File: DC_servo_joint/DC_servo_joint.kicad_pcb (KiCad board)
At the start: 2 copper layers, 6 parts, among them J1 12401598E4_2A, J2 B2B-XH-A_LF__SN_, U1 DRV8871DDA, U2 ESP32-C3-WROOM-02, U3 MT6701CT, U4 LM1117MP-3.3

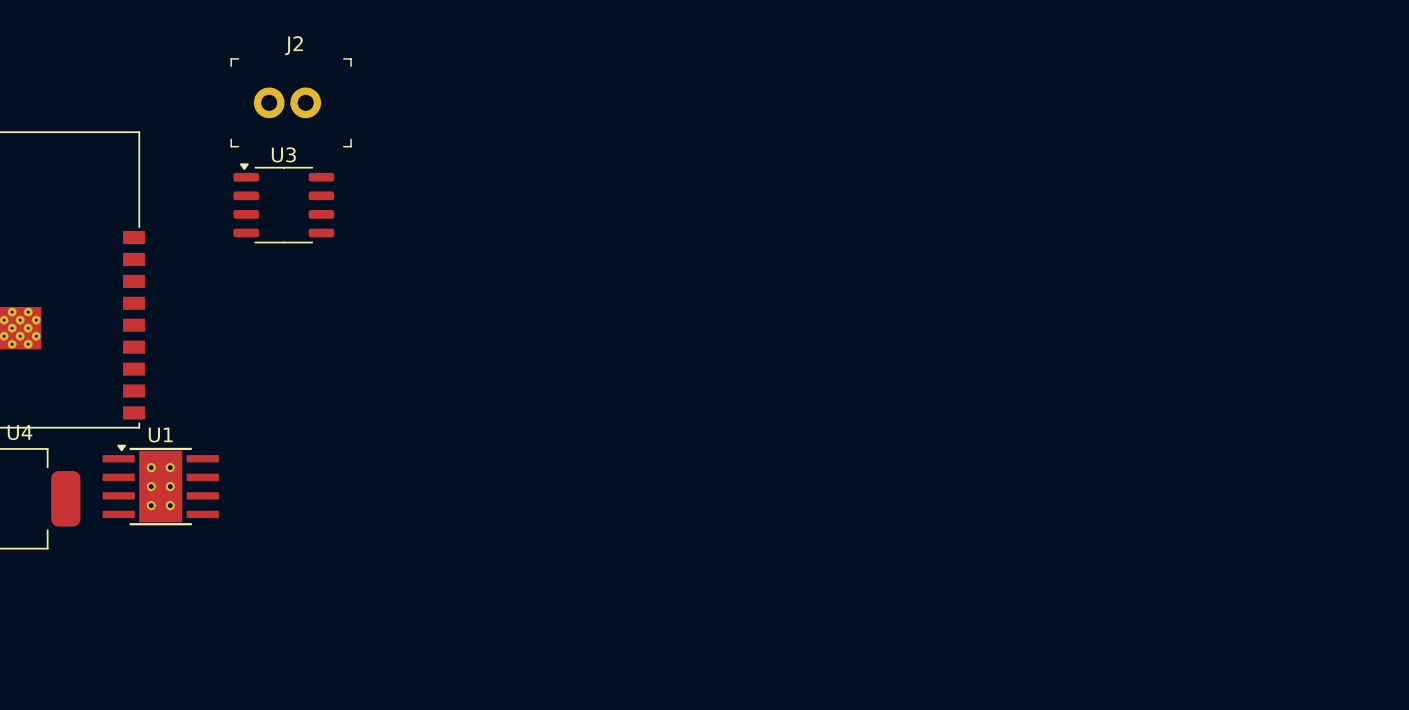
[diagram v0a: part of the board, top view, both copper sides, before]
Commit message: Update the usb header to 8 pins,
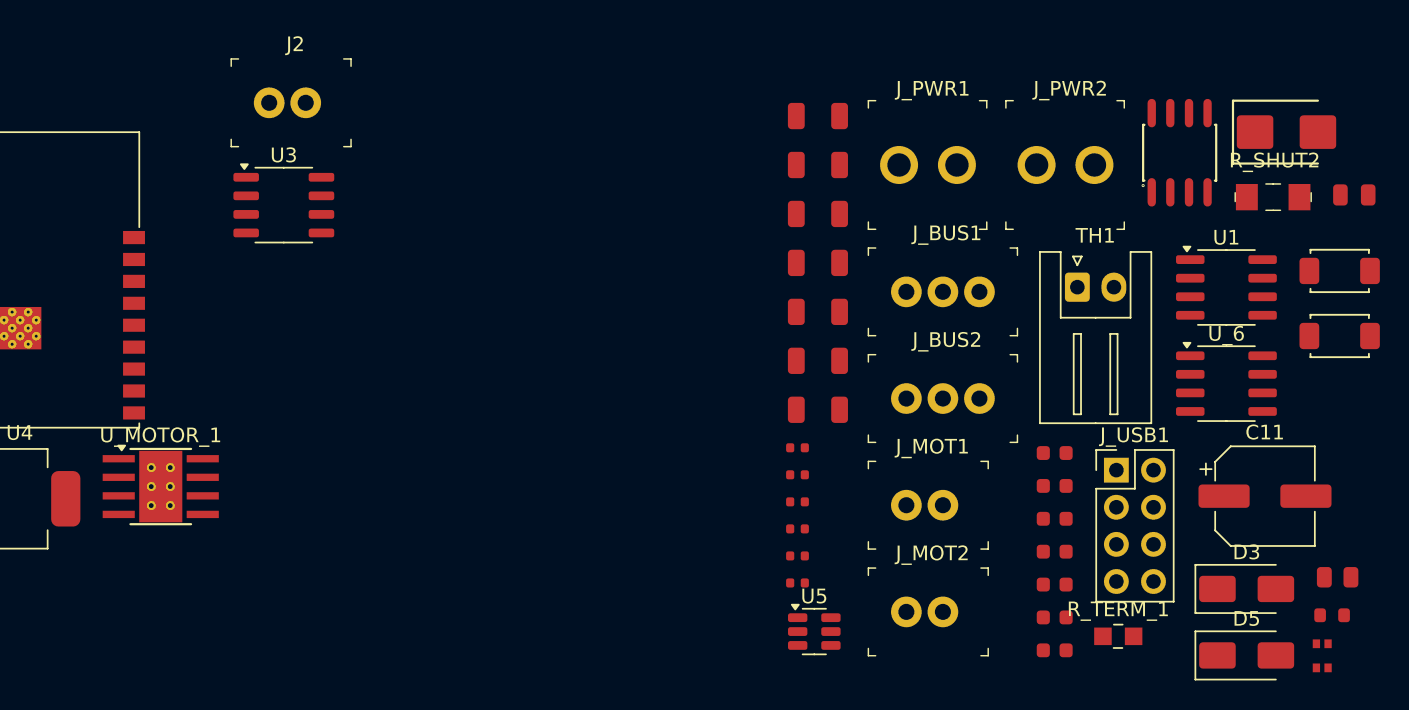
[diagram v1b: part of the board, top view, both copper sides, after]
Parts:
- added C1: 4.7uF, PCM_JLCPCB:C_1206, F.Cu at (190.6, 77.7)
- added C10: 22uF, PCM_JLCPCB:C_1206, F.Cu at (190.6, 94.5)
- added C11: 47uf, Capacitor_SMD:CP_Elec_6.3x5.4, F.Cu at (221.2, 103.8)
- added C12: 100nF, PCM_JLCPCB:C_0603, F.Cu at (206.8, 109.8)
- added C13: 100nF, PCM_JLCPCB:C_0603, F.Cu at (206.8, 112.0)
- added C14: 10uF, PCM_JLCPCB:C_0805, F.Cu at (227.3, 83.1)
- added C16: 100nF, PCM_JLCPCB:C_0603, F.Cu at (206.8, 114.3)
- added C17: 4.7uF, PCM_JLCPCB:C_1206, F.Cu at (190.6, 97.8)
- added C2: 220nF, PCM_JLCPCB:C_1206, F.Cu at (190.6, 81.1)
- added C3: 22uF, PCM_JLCPCB:C_1206, F.Cu at (190.6, 84.4)
- added C4: 100nF, PCM_JLCPCB:C_0603, F.Cu at (206.8, 100.8)
- added C5: 100nF, PCM_JLCPCB:C_1206, F.Cu at (190.6, 87.8)
- added C6: 100nF, PCM_JLCPCB:C_0603, F.Cu at (206.8, 103.0)
- added C7: 100nF, PCM_JLCPCB:C_0603, F.Cu at (206.8, 105.3)
- added C8: 10nF, PCM_JLCPCB:C_0603, F.Cu at (206.8, 107.5)
- added C9: 10uF, PCM_JLCPCB:C_1206, F.Cu at (190.6, 91.1)
- added D1: SMBJ6.5CA, PCM_JLCPCB:D_SMB, F.Cu at (222.7, 78.8)
- added D2: H15VL10B, PCM_JLCPCB:D_DFN1006-2L, F.Cu at (225.1, 113.8)
- added D3: SS34, Diode_SMD:D_SMA, F.Cu at (219.9, 110.1)
- added D4: H15VL10B, PCM_JLCPCB:D_DFN1006-2L, F.Cu at (225.1, 115.5)
- added D5: SS34, Diode_SMD:D_SMA, F.Cu at (219.9, 114.7)
- added J_BUS1: B3B-XH-A_LF__SN_, digikey-footprints:PinHeader_1x3_P2.5mm_Drill1.1mm, F.Cu at (196.6, 89.8)
- added J_BUS2: B3B-XH-A_LF__SN_, digikey-footprints:PinHeader_1x3_P2.5mm_Drill1.1mm, F.Cu at (196.6, 97.1)
- added J_MOT1: B2B-XH-A_LF__SN_, digikey-footprints:PinHeader_1x2_P2.5mm_Drill1.1mm, F.Cu at (196.6, 104.4)
- added J_MOT2: B2B-XH-A_LF__SN_, digikey-footprints:PinHeader_1x2_P2.5mm_Drill1.1mm, F.Cu at (196.6, 111.7)
- added J_PWR1: B2P-VH_LF__SN_, digikey-footprints:PinHeader_1x2_P3.96mm_Drill1.6mm, F.Cu at (196.1, 81.1)
- added J_PWR2: B2P-VH_LF__SN_, digikey-footprints:PinHeader_1x2_P3.96mm_Drill1.6mm, F.Cu at (205.6, 81.1)
- added J_USB1: USB_PAD, Connector_PinHeader_2.54mm:PinHeader_2x04_P2.54mm_Vertical, F.Cu at (211.0, 102.0)
- added R1: 33kΩ, PCM_JLCPCB:R_0402, F.Cu at (189.2, 100.4)
- added R2: 10kΩ, PCM_JLCPCB:R_0402, F.Cu at (189.2, 102.3)
- added R3: 68kΩ, PCM_JLCPCB:R_0805, F.Cu at (226.2, 109.3)
- added R4: 10kΩ, PCM_JLCPCB:R_0603, F.Cu at (225.8, 111.9)
- added R5: 10kΩ, PCM_JLCPCB:R_0402, F.Cu at (189.2, 104.1)
- added R7: 10kΩ, PCM_JLCPCB:R_0402, F.Cu at (189.2, 106.0)
- added R_SHUT2: 0.05ohm, digikey-footprints:1206, F.Cu at (221.7, 83.3)
- added R_TERM_1: 120, digikey-footprints:0805, F.Cu at (211.1, 113.3)
- added R_i2c1: 4.7kΩ, PCM_JLCPCB:R_0402, F.Cu at (189.2, 107.8)
- added R_i2c2: 4.7kΩ, PCM_JLCPCB:R_0402, F.Cu at (189.2, 109.7)
- added S1: RST_BTM, PCM_JLCPCB:SW_TS-1088-AR02016, F.Cu at (226.3, 88.3)
- added S2: BOOT_BTM, PCM_JLCPCB:SW_TS-1088-AR02016, F.Cu at (226.3, 92.8)
- added TH1: NTC 10K, Connector_JST:JST_XH_S2B-XH-A_1x02_P2.50mm_Horizontal, F.Cu at (208.3, 89.5)
- added U1: AS5600, Package_SO:SOIC-8_3.9x4.9mm_P1.27mm, F.Cu at (218.5, 89.5)
- added U3: SP3485EN, PCM_JLCPCB:SOIC-8_L5.0-W4.0-P1.27-LS6.0-BL, F.Cu at (215.3, 80.2)
- added U5: TPS563200, Package_TO_SOT_SMD:SOT-23-6, F.Cu at (190.3, 113.0)
- added U_6: INA219BxD, Package_SO:SOIC-8_3.9x4.9mm_P1.27mm, F.Cu at (218.5, 96.0)
- renumbered U1 to U_MOTOR_1
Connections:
- U2 pad 1: unconnected-(U2-3V3-Pad1) -> +3.3V
- U2 pad 15: unconnected-(U2-IO3-Pad15) -> /pwm2_io3
- U2 pad 16: unconnected-(U2-IO2-Pad16) -> /pwm1_io2
- U2 pad 18: unconnected-(U2-IO0-Pad18) -> /NTC_PIN
- U2 pad 19: Net-(U2-GND-Pad19) -> GND
- U2 pad 2: unconnected-(U2-EN-Pad2) -> /RST_BTM
- U2 pad 3: unconnected-(U2-IO4-Pad3) -> /SCL
- U2 pad 4: unconnected-(U2-IO5-Pad4) -> /SDA
- U2 pad 5: unconnected-(U2-IO6-Pad5) -> /UART_TX
- U2 pad 6: unconnected-(U2-IO7-Pad6) -> /UART_RX
- U2 pad 7: unconnected-(U2-IO8-Pad7) -> /485_RE_DE
- U2 pad 8: unconnected-(U2-IO9-Pad8) -> /BOOT_BTM
- U2 pad 9: Net-(U2-GND-Pad19) -> GND
- U_MOTOR_1 pad 1: Net-(U1-GND-Pad1) -> GND
- U_MOTOR_1 pad 2: unconnected-(U1-IN2-Pad2) -> /pwm2_io3
- U_MOTOR_1 pad 3: unconnected-(U1-IN1-Pad3) -> /pwm1_io2
- U_MOTOR_1 pad 4: unconnected-(U1-ILIM-Pad4) -> Net-(U_MOTOR_1-ILIM)
- U_MOTOR_1 pad 5: unconnected-(U1-VM-Pad5) -> Net-(U_6-IN-)
- U_MOTOR_1 pad 6: unconnected-(U1-OUT1-Pad6) -> Net-(U_MOTOR_1-OUT1)
- U_MOTOR_1 pad 7: Net-(U1-GND-Pad1) -> GND
- U_MOTOR_1 pad 8: unconnected-(U1-OUT2-Pad8) -> Net-(U_MOTOR_1-OUT2)
- U_MOTOR_1 pad 9: Net-(U1-GND-Pad1) -> GND

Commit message: Started Power source layout
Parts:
- removed J1: 12401598E4_2A, digikey-footprints:USB-C_Female_12401X
- removed J2, J_MOT2: B2B-XH-A_LF__SN_, digikey-footprints:PinHeader_1x2_P2.5mm_Drill1.1mm
- removed the U3 at (154.0, 83.8)
- removed U4: LM1117MP-3.3, Package_TO_SOT_SMD:SOT-223-3_TabPin2
- added L2: 2.2uH,50mA, PCM_JLCPCB:L_0805, F.Cu at (181.8, 128.1)
- moved U_6 126.5 mm to (94.0, 74.0)
- moved U1 121.8 mm to (99.5, 63.5)
- moved S2 118.7 mm to (108.5, 78.0)
- moved S1 118.4 mm to (108.0, 84.5)
- moved C14 111.7 mm to (125.0, 128.0)
- moved J_PWR1 110.7 mm to (92.5, 120.0)
- moved R3 97.6 mm to (129.0, 119.0)
- moved R_TERM_1 94.8 mm to (122.0, 81.0)
- moved U3 90.1 mm to (125.6, 72.8)
- moved C4 87.8 mm to (119.0, 103.0)
- moved D2 81.1 mm to (144.0, 112.0)
- moved C7 81.0 mm to (129.0, 128.0)
- moved R_SHUT2 79.2 mm to (155.0, 126.0)
- moved C8 77.5 mm to (132.0, 128.0)
- moved C6 76.0 mm to (135.0, 128.0)
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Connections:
- net Net-(U5-SW) renamed /TPS_SW
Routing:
- net +3.3V: track 0.00 -> 8.47 mm
- net GND: track 0.00 -> 7.56 mm
- net Net-(U5-VFB): track 0.00 -> 3.95 mm
- net Net-(U5-EN): track 0.00 -> 3.87 mm
- net /V_IN: track 0.00 -> 2.28 mm
- net /TPS_SW: track 0.00 -> 1.86 mm, vias 0 -> 3
- added copper zone on F.Cu, net +3.3V
- added copper zone on B.Cu, net /TPS_SW
- added copper zone on F.Cu, net /V_IN
- added copper zone on F.Cu, net GND
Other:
- board outline added: 93 x 83.5 mm

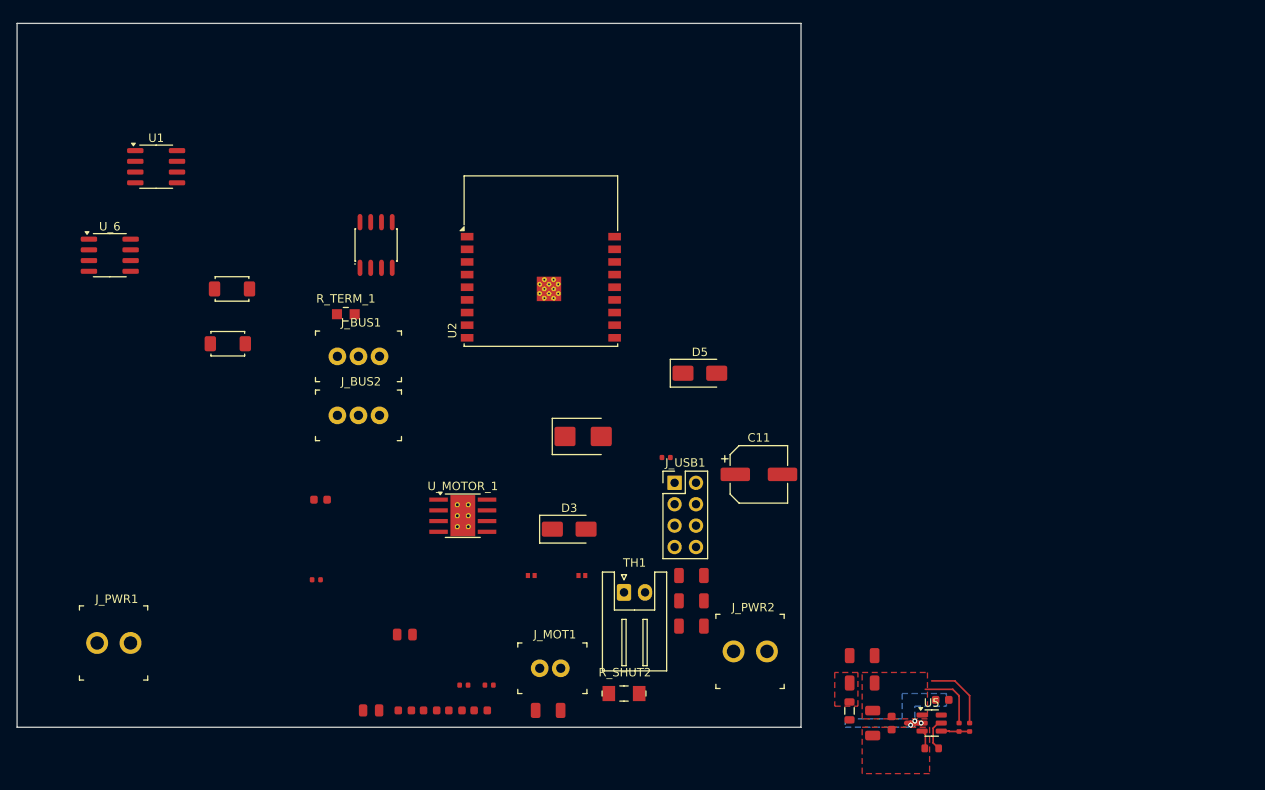
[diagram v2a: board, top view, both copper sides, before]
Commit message: Most layout are in shape
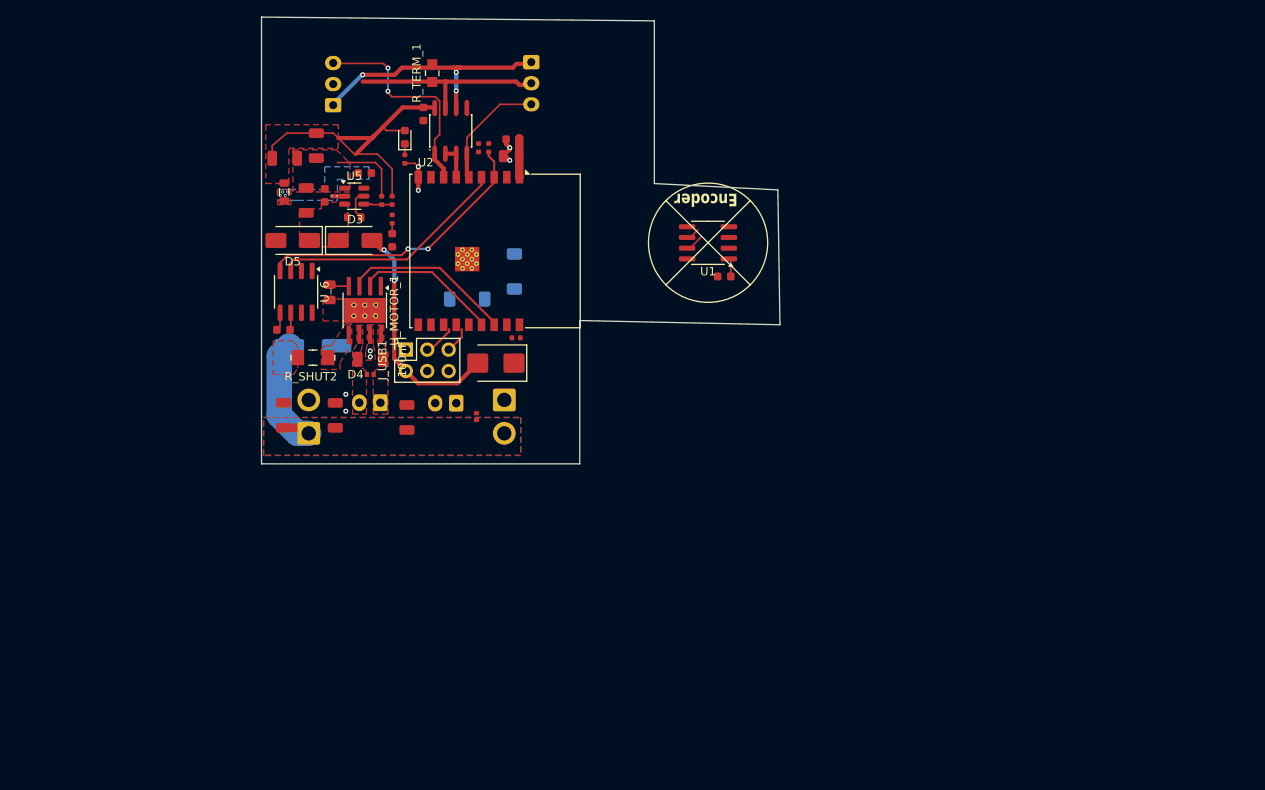
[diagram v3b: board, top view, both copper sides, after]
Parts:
- added D6: Red, PCM_JLCPCB:D_0603, F.Cu at (129.0, 60.0)
- added R6: 1kΩ, PCM_JLCPCB:R_0402, F.Cu at (129.0, 62.6)
- C11, S1, S2, TH1: moved to B.Cu
- J_BUS1, J_BUS2: footprint digikey-footprints:PinHeader_1x3_P2.5mm_Drill1.1mm -> Connector_JST:JST_XH_S3B-XH-A_1x03_P2.50mm_Horizontal; moved to B.Cu
- J_MOT1: footprint digikey-footprints:PinHeader_1x2_P2.5mm_Drill1.1mm -> Connector_JST:JST_XH_S2B-XH-A_1x02_P2.50mm_Horizontal; moved to B.Cu
- J_PWR1, J_PWR2: footprint digikey-footprints:PinHeader_1x2_P3.96mm_Drill1.6mm -> Connector_JST:JST_VH_S2P-VH_1x02_P3.96mm_Horizontal; moved to B.Cu
- J_USB1: footprint Connector_PinHeader_2.54mm:PinHeader_2x04_P2.54mm_Vertical -> Connector_PinSocket_2.54mm:PinSocket_2x03_P2.54mm_Vertical
- moved R4 93.1 mm to (123.0, 69.5)
- moved C13 92.7 mm to (124.2, 64.2)
- moved R1 92.7 mm to (127.5, 67.5)
- moved R7 92.7 mm to (126.2, 67.5)
- moved U5 92.7 mm to (123.0, 67.0)
- moved C3 92.6 mm to (114.8, 62.5)
- moved C12 91.9 mm to (119.5, 66.9)
- moved C9 91.4 mm to (117.3, 67.5)
- moved L2 91.0 mm to (114.7, 66.5)
- moved C10 88.6 mm to (118.5, 61.0), turned to -90 degrees
- moved C16 71.1 mm to (131.2, 57.2), turned to -90 degrees
- moved C8 68.5 mm to (141.8, 60.2), turned to 180 degrees
- moved C14 67.8 mm to (141.6, 62.2), turned to 180 degrees
- moved U1 66.1 mm to (165.0, 72.5), turned to 180 degrees
- moved C7 63.9 mm to (166.9, 76.5), turned to 180 degrees
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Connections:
- net Net-(U_6-IN-) renamed /V_motor
- net Net-(U_MOTOR_1-OUT1) renamed /Mot1
- net Net-(U_MOTOR_1-OUT2) renamed /Mot2
- J_PWR2 pad 1: +12V -> GND
- J_PWR2 pad 2: GND -> +12V
- J_USB1 pad 3: /D+ -> /D-
- J_USB1 pad 5: /D- -> /D+
- J_USB1 pad 6: unconnected-(J_USB1-Pin_6-Pad6) -> GND
- U2 pad 6: /UART_RX -> /485_RE_DE
- U2 pad 7: /485_RE_DE -> /UART_RX
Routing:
- net +3.3V: track 8.47 -> 48.9 mm
- net /SCL: track 0.00 -> 35.9 mm, vias 0 -> 2
- net /RS485A: track 0.00 -> 31.8 mm, vias 0 -> 3
- net /SDA: track 0.00 -> 30.6 mm
- net /usb_5v: track 0.00 -> 27.5 mm, vias 0 -> 2
- net /UART_RX: track 0.00 -> 25.7 mm, vias 0 -> 2
- net /RS485B: track 0.00 -> 23.3 mm
- net /pwm1_io2: track 0.00 -> 20.3 mm
- net /pwm2_io3: track 0.00 -> 17.1 mm
- net +12V: track 0.00 -> 16.4 mm
- net /UART_TX: track 0.00 -> 14.1 mm
- net GND: track 7.56 -> 19.3 mm, vias 0 -> 8
- net /485_RE_DE: track 0.00 -> 4.09 mm
- net /D-: track 0.00 -> 3.71 mm
- net /D+: track 0.00 -> 3.07 mm
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- added copper zone on B.Cu, net +12V
- added copper zone on F.Cu, net +12V
- added copper zone on F.Cu, net /Mot1
- added copper zone on F.Cu, net /Mot2
- added copper zone on F.Cu, net /TPS_SW
- added copper zone on F.Cu, net /V_motor
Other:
- board size 93 x 83.5 mm -> 61.5 x 53 mm
- board text added: "Encoder"

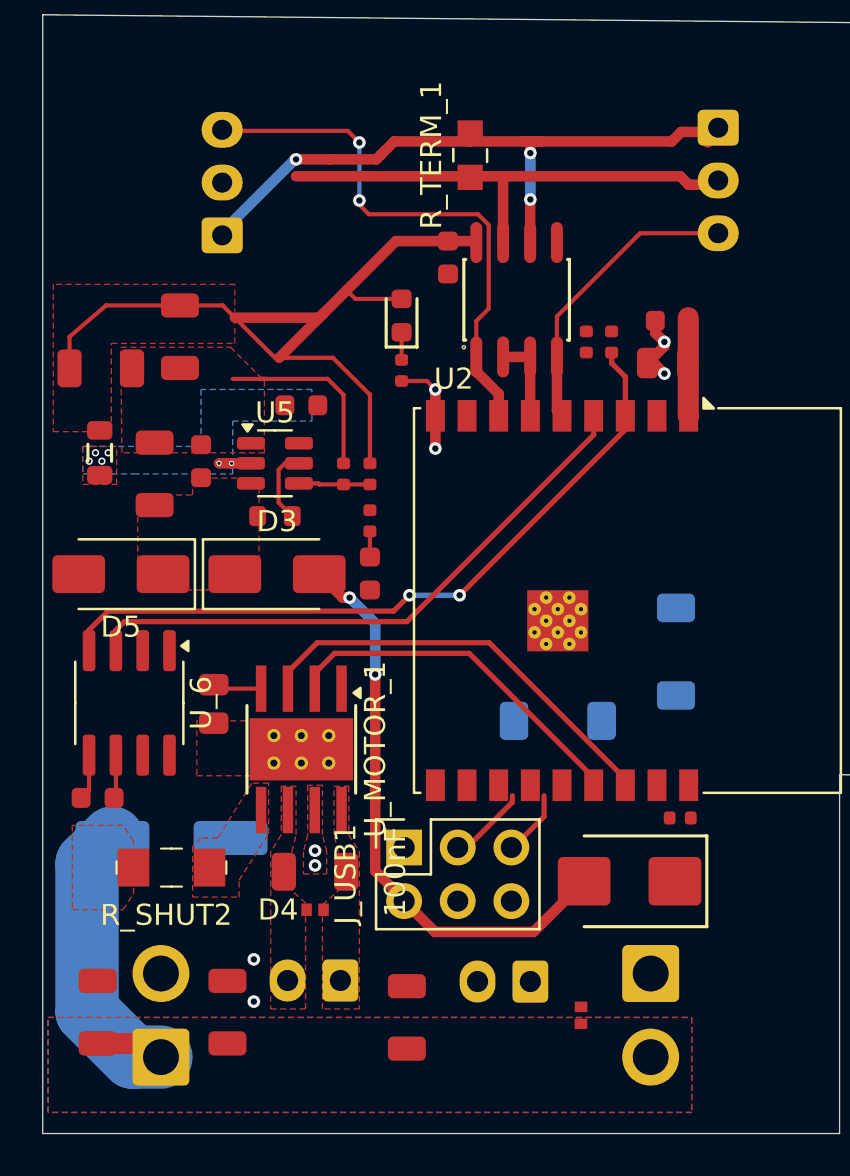
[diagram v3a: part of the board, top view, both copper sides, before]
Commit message: Finalize button placement
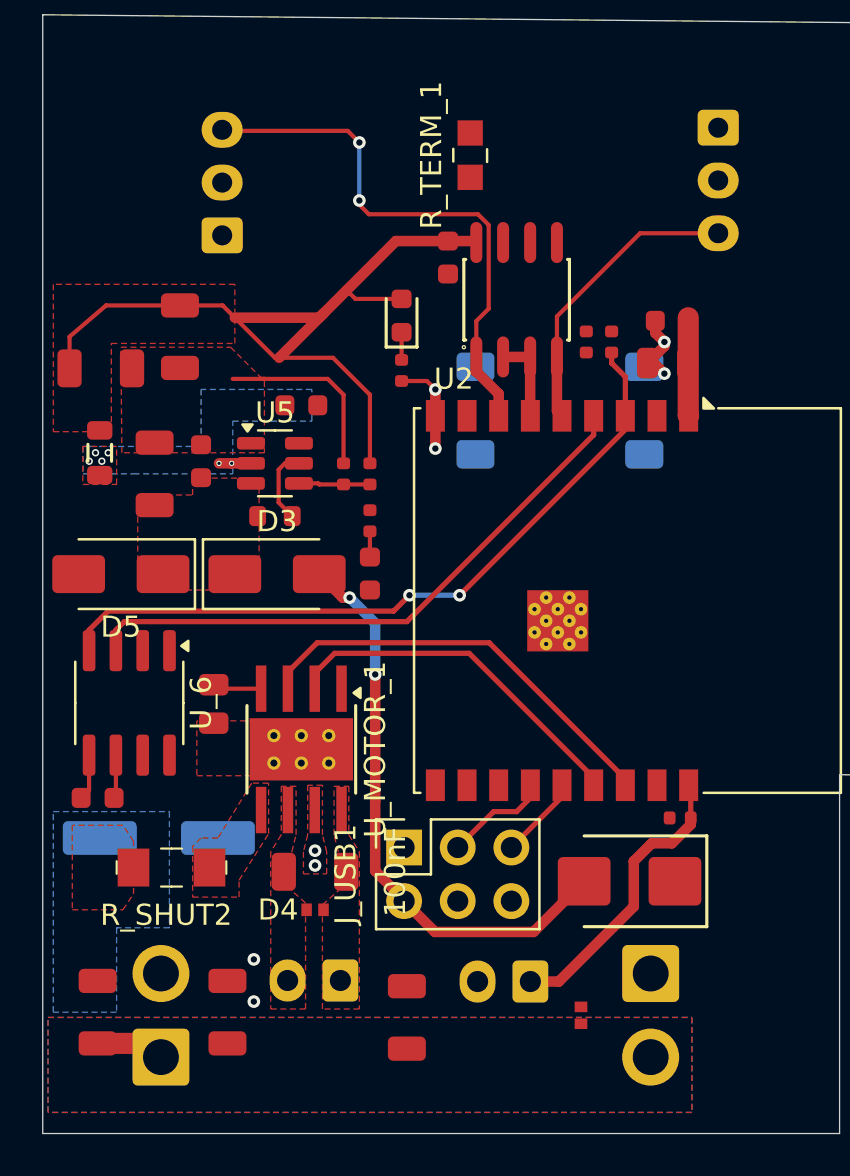
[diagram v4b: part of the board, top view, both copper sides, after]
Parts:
- moved S1 15.3 mm to (140.5, 64.5), turned to 90 degrees
- moved S2 14.9 mm to (132.5, 64.5)
- moved C11 0.60 mm to (117.5, 84.8)
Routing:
- net /RS485A: track 31.8 -> 0.00 mm, vias 3 -> 0
- net /RS485B: track 23.3 -> 0.00 mm
- net /NTC_PIN: track 0.00 -> 13.8 mm
- net +12V: track 16.4 -> 3.27 mm
- net /D-: track 3.71 -> 5.01 mm
- net /D+: track 3.07 -> 3.94 mm
